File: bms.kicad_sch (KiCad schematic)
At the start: 58 parts, among them J6 TYPE-C_16PIN_2MD__073_, J7 Battery, Q2 PMOS, Q3 PMOS, U3 TPS2113ADRBR, U6 MP2639A, U8 LMV331M5, U9 LMV331M5

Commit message: changed most of the components to 0805
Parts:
- C20, C50, C51, C53: footprint Capacitor_SMD:C_0603_1608Metric_Pad1.08x0.95mm_HandSolder -> Capacitor_SMD:C_0805_2012Metric_Pad1.18x1.45mm_HandSolder
- C35, C38, C42, C43: footprint Capacitor_SMD:C_0402_1005Metric_Pad0.74x0.62mm_HandSolder -> Capacitor_SMD:C_0805_2012Metric_Pad1.18x1.45mm_HandSolder
- D3, D4, D5, D6, D7, D8: footprint LED_SMD:LED_0402_1005Metric_Pad0.77x0.64mm_HandSolder -> LED_SMD:LED_0805_2012Metric_Pad1.15x1.40mm_HandSolder
- R17, R18, R19, R20, R21, R22, R23, R24, R25, R31, R32, R33, R34, R39, R40, R41, R42, R43, R44, R45, R46, R47, R48, R49, R50, R51: footprint Resistor_SMD:R_0402_1005Metric_Pad0.72x0.64mm_HandSolder -> Resistor_SMD:R_0805_2012Metric_Pad1.20x1.40mm_HandSolder
- R26: footprint Resistor_SMD:R_0603_1608Metric_Pad0.98x0.95mm_HandSolder -> Resistor_SMD:R_0805_2012Metric_Pad1.20x1.40mm_HandSolder
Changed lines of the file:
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@@
 	)
 	(junction
+		(at 236.22 101.6)
+		(diameter 0)
+		(color 0 0 0 0)
+	)
+	(junction
 		(at 88.9 24.13)
 		(diameter 0)
@@
 	(wire
 		(pts
+			(xy 236.22 101.6) (xy 238.76 101.6)
+		)
+		(stroke
+			(width 0)
+			(type default)
+		)
+	)
+	(wire
+		(pts
 			(xy 20.32 44.45) (xy 20.32 40.64)
 		)
@@
 			)
 		)
-		(property "Footprint" "Capacitor_SMD:C_0603_1608Metric_Pad1.08x0.95mm_HandSolder"
+		(property "Footprint" "Capacitor_SMD:C_0805_2012Metric_Pad1.18x1.45mm_HandSolder"
 			(at 121.92 132.08 0)
 			(hide yes)
@@
 			)
 		)
-		(property "Footprint" "Resistor_SMD:R_0402_1005Metric_Pad0.72x0.64mm_HandSolder"
+		(property "Footprint" "Resistor_SMD:R_0805_2012Metric_Pad1.20x1.40mm_HandSolder"
 			(at 99.06 59.69 0)
 			(hide yes)
@@
 			)
 		)
-		(property "Footprint" "Resistor_SMD:R_0402_1005Metric_Pad0.72x0.64mm_HandSolder"
+		(property "Footprint" "Resistor_SMD:R_0805_2012Metric_Pad1.20x1.40mm_HandSolder"
 			(at 99.06 66.04 0)
 			(hide yes)
@@
 			)
 		)
-		(property "Footprint" "Capacitor_SMD:C_0402_1005Metric_Pad0.74x0.62mm_HandSolder"
+		(property "Footprint" "Capacitor_SMD:C_0805_2012Metric_Pad1.18x1.45mm_HandSolder"
 			(at 265.43 88.9 0)
 			(hide yes)
@@
 			)
 		)
-		(property "Footprint" "Capacitor_SMD:C_0402_1005Metric_Pad0.74x0.62mm_HandSolder"
+		(property "Footprint" "Capacitor_SMD:C_0805_2012Metric_Pad1.18x1.45mm_HandSolder"
 			(at 154.94 49.53 0)
 			(hide yes)
@@
 			)
 		)
-		(property "Footprint" "Resistor_SMD:R_0603_1608Metric_Pad0.98x0.95mm_HandSolder"
+		(property "Footprint" "Resistor_SMD:R_0805_2012Metric_Pad1.20x1.40mm_HandSolder"
 			(at 71.12 46.99 0)
 			(hide yes)
@@
 			)
 		)
-		(property "Footprint" "Capacitor_SMD:C_0402_1005Metric_Pad0.74x0.62mm_HandSolder"
+		(property "Footprint" "Capacitor_SMD:C_0805_2012Metric_Pad1.18x1.45mm_HandSolder"
 			(at 151.13 66.04 0)
 			(hide yes)
@@
 			)
 		)
-		(property "Footprint" "Resistor_SMD:R_0402_1005Metric_Pad0.72x0.64mm_HandSolder"
+		(property "Footprint" "Resistor_SMD:R_0805_2012Metric_Pad1.20x1.40mm_HandSolder"
 			(at 101.6 74.93 0)
 			(hide yes)
@@
 			)
 		)
-		(property "Footprint" "Capacitor_SMD:C_0603_1608Metric_Pad1.08x0.95mm_HandSolder"
+		(property "Footprint" "Capacitor_SMD:C_0805_2012Metric_Pad1.18x1.45mm_HandSolder"
 			(at 134.62 85.09 0)
 			(hide yes)
@@
 			)
 		)
-		(property "Footprint" "Resistor_SMD:R_0402_1005Metric_Pad0.72x0.64mm_HandSolder"
+		(property "Footprint" "Resistor_SMD:R_0805_2012Metric_Pad1.20x1.40mm_HandSolder"
 			(at 236.22 152.4 0)
 			(hide yes)
@@
 			)
 		)
-		(property "Footprint" "Resistor_SMD:R_0402_1005Metric_Pad0.72x0.64mm_HandSolder"
+		(property "Footprint" "Resistor_SMD:R_0805_2012Metric_Pad1.20x1.40mm_HandSolder"
 			(at 187.96 31.75 0)
 			(hide yes)
@@
 			)
 		)
-		(property "Footprint" "LED_SMD:LED_0402_1005Metric_Pad0.77x0.64mm_HandSolder"
+		(property "Footprint" "LED_SMD:LED_0805_2012Metric_Pad1.15x1.40mm_HandSolder"
 			(at 81.28 85.09 0)
 			(hide yes)
@@
 			)
 		)
-		(property "Footprint" "Resistor_SMD:R_0402_1005Metric_Pad0.72x0.64mm_HandSolder"
+		(property "Footprint" "Resistor_SMD:R_0805_2012Metric_Pad1.20x1.40mm_HandSolder"
 			(at 218.44 88.9 0)
 			(hide yes)
@@
 			)
 		)
-		(property "Footprint" "Resistor_SMD:R_0402_1005Metric_Pad0.72x0.64mm_HandSolder"
+		(property "Footprint" "Resistor_SMD:R_0805_2012Metric_Pad1.20x1.40mm_HandSolder"
 			(at 256.54 138.43 0)
 			(hide yes)
@@
 			)
 		)
-		(property "Footprint" "LED_SMD:LED_0402_1005Metric_Pad0.77x0.64mm_HandSolder"
+		(property "Footprint" "LED_SMD:LED_0805_2012Metric_Pad1.15x1.40mm_HandSolder"
 			(at 83.82 55.88 0)
 			(hide yes)
@@
 			)
 		)
-		(property "Footprint" "Resistor_SMD:R_0402_1005Metric_Pad0.72x0.64mm_HandSolder"
+		(property "Footprint" "Resistor_SMD:R_0805_2012Metric_Pad1.20x1.40mm_HandSolder"
 			(at 148.59 46.99 0)
 			(hide yes)
@@
 			)
 		)
-		(property "Footprint" "Resistor_SMD:R_0402_1005Metric_Pad0.72x0.64mm_HandSolder"
+		(property "Footprint" "Resistor_SMD:R_0805_2012Metric_Pad1.20x1.40mm_HandSolder"
 			(at 99.06 55.88 0)
 			(hide yes)
@@
 			)
 		)
-		(property "Footprint" "Resistor_SMD:R_0402_1005Metric_Pad0.72x0.64mm_HandSolder"
+		(property "Footprint" "Resistor_SMD:R_0805_2012Metric_Pad1.20x1.40mm_HandSolder"
 			(at 210.82 120.65 0)
 			(hide yes)
@@
 			)
 		)
-		(property "Footprint" "Resistor_SMD:R_0402_1005Metric_Pad0.72x0.64mm_HandSolder"
+		(property "Footprint" "Resistor_SMD:R_0805_2012Metric_Pad1.20x1.40mm_HandSolder"
 			(at 187.96 36.83 0)
 			(hide yes)
@@
 			)
 		)
-		(property "Footprint" "Resistor_SMD:R_0402_1005Metric_Pad0.72x0.64mm_HandSolder"
+		(property "Footprint" "Resistor_SMD:R_0805_2012Metric_Pad1.20x1.40mm_HandSolder"
 			(at 210.82 148.59 0)
 			(hide yes)
@@
 			)
 		)
-		(property "Footprint" "Resistor_SMD:R_0402_1005Metric_Pad0.72x0.64mm_HandSolder"
+		(property "Footprint" "Resistor_SMD:R_0805_2012Metric_Pad1.20x1.40mm_HandSolder"
 			(at 62.23 50.8 0)
 			(hide yes)
@@
 		(pin "9"
 		)
+		(pin "9"
+		)
 		(instances
 			(project "STM32G491RE"
@@
 			)
 		)
-		(property "Footprint" "Resistor_SMD:R_0402_1005Metric_Pad0.72x0.64mm_HandSolder"
+		(property "Footprint" "Resistor_SMD:R_0805_2012Metric_Pad1.20x1.40mm_HandSolder"
 			(at 125.73 144.78 0)
 			(hide yes)
@@
 			)
 		)
-		(property "Footprint" "LED_SMD:LED_0402_1005Metric_Pad0.77x0.64mm_HandSolder"
+		(property "Footprint" "LED_SMD:LED_0805_2012Metric_Pad1.15x1.40mm_HandSolder"
 			(at 83.82 62.23 0)
 			(hide yes)
@@
 			)
 		)
-		(property "Footprint" "Resistor_SMD:R_0402_1005Metric_Pad0.72x0.64mm_HandSolder"
+		(property "Footprint" "Resistor_SMD:R_0805_2012Metric_Pad1.20x1.40mm_HandSolder"
 			(at 236.22 124.46 0)
 			(hide yes)
@@
 			)
 		)
-		(property "Footprint" "LED_SMD:LED_0402_1005Metric_Pad0.77x0.64mm_HandSolder"
+		(property "Footprint" "LED_SMD:LED_0805_2012Metric_Pad1.15x1.40mm_HandSolder"
 			(at 83.82 66.04 0)
 			(hide yes)
@@
 			)
 		)
-		(property "Footprint" "Resistor_SMD:R_0402_1005Metric_Pad0.72x0.64mm_HandSolder"
+		(property "Footprint" "Resistor_SMD:R_0805_2012Metric_Pad1.20x1.40mm_HandSolder"
 			(at 146.05 63.5 0)
 			(hide yes)
@@
 			)
 		)
-		(property "Footprint" "Resistor_SMD:R_0402_1005Metric_Pad0.72x0.64mm_HandSolder"
+		(property "Footprint" "Resistor_SMD:R_0805_2012Metric_Pad1.20x1.40mm_HandSolder"
 			(at 161.29 64.77 0)
 			(hide yes)
@@
 			)
 		)
-		(property "Footprint" "Resistor_SMD:R_0402_1005Metric_Pad0.72x0.64mm_HandSolder"
+		(property "Footprint" "Resistor_SMD:R_0805_2012Metric_Pad1.20x1.40mm_HandSolder"
 			(at 161.29 59.69 0)
 			(hide yes)
@@
 			)
 		)
-		(property "Footprint" "Resistor_SMD:R_0402_1005Metric_Pad0.72x0.64mm_HandSolder"
+		(property "Footprint" "Resistor_SMD:R_0805_2012Metric_Pad1.20x1.40mm_HandSolder"
 			(at 250.19 132.08 0)
 			(hide yes)
@@
 			)
 		)
-		(property "Footprint" "LED_SMD:LED_0402_1005Metric_Pad0.77x0.64mm_HandSolder"
+		(property "Footprint" "LED_SMD:LED_0805_2012Metric_Pad1.15x1.40mm_HandSolder"
 			(at 81.28 80.01 0)
 			(hide yes)
@@
 			)
 		)
-		(property "Footprint" "Resistor_SMD:R_0402_1005Metric_Pad0.72x0.64mm_HandSolder"
+		(property "Footprint" "Resistor_SMD:R_0805_2012Metric_Pad1.20x1.40mm_HandSolder"
 			(at 181.61 128.27 0)
 			(hide yes)
@@
 			)
 		)
-		(property "Footprint" "Capacitor_SMD:C_0603_1608Metric_Pad1.08x0.95mm_HandSolder"
+		(property "Footprint" "Capacitor_SMD:C_0805_2012Metric_Pad1.18x1.45mm_HandSolder"
 			(at 88.9 21.59 0)
 			(hide yes)
@@
 			)
 		)
-		(property "Footprint" "Resistor_SMD:R_0402_1005Metric_Pad0.72x0.64mm_HandSolder"
+		(property "Footprint" "Resistor_SMD:R_0805_2012Metric_Pad1.20x1.40mm_HandSolder"
 			(at 163.83 144.78 0)
 			(hide yes)
@@
 			)
 		)
-		(property "Footprint" "Resistor_SMD:R_0402_1005Metric_Pad0.72x0.64mm_HandSolder"
+		(property "Footprint" "Resistor_SMD:R_0805_2012Metric_Pad1.20x1.40mm_HandSolder"
 			(at 105.41 76.2 0)
 			(hide yes)
@@
 			)
 		)
-		(property "Footprint" "LED_SMD:LED_0402_1005Metric_Pad0.77x0.64mm_HandSolder"
+		(property "Footprint" "LED_SMD:LED_0805_2012Metric_Pad1.15x1.40mm_HandSolder"
 			(at 83.82 59.69 0)
 			(hide yes)
@@
 			)
 		)
-		(property "Footprint" "Capacitor_SMD:C_0402_1005Metric_Pad0.74x0.62mm_HandSolder"
+		(property "Footprint" "Capacitor_SMD:C_0805_2012Metric_Pad1.18x1.45mm_HandSolder"
 			(at 257.81 88.9 0)
 			(hide yes)
@@
 			)
 		)
-		(property "Footprint" "Resistor_SMD:R_0402_1005Metric_Pad0.72x0.64mm_HandSolder"
+		(property "Footprint" "Resistor_SMD:R_0805_2012Metric_Pad1.20x1.40mm_HandSolder"
 			(at 146.05 66.04 0)
 			(hide yes)
@@
 			)
 		)
-		(property "Footprint" "Resistor_SMD:R_0402_1005Metric_Pad0.72x0.64mm_HandSolder"
+		(property "Footprint" "Resistor_SMD:R_0805_2012Metric_Pad1.20x1.40mm_HandSolder"
 			(at 181.61 133.35 0)
 			(hide yes)
@@
 			)
 		)
-		(property "Footprint" "Resistor_SMD:R_0402_1005Metric_Pad0.72x0.64mm_HandSolder"
+		(property "Footprint" "Resistor_SMD:R_0805_2012Metric_Pad1.20x1.40mm_HandSolder"
 			(at 99.06 62.23 0)
 			(hide yes)
@@
 			)
 		)
-		(property "Footprint" "Resistor_SMD:R_0402_1005Metric_Pad0.72x0.64mm_HandSolder"
+		(property "Footprint" "Resistor_SMD:R_0805_2012Metric_Pad1.20x1.40mm_HandSolder"
 			(at 148.59 44.45 0)
 			(hide yes)
@@
 			)
 		)
-		(property "Footprint" "Capacitor_SMD:C_0603_1608Metric_Pad1.08x0.95mm_HandSolder"
+		(property "Footprint" "Capacitor_SMD:C_0805_2012Metric_Pad1.18x1.45mm_HandSolder"
 			(at 36.83 46.99 0)
 			(hide yes)

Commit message: finalized parts before sensors
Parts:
- removed C59: 22uF, Capacitor_SMD:C_1206_3216Metric_Pad1.33x1.80mm_HandSolder, symbol Device:C_Small
- C51: footprint Capacitor_SMD:C_0805_2012Metric_Pad1.18x1.45mm_HandSolder -> Capacitor_SMD:C_0603_1608Metric_Pad1.08x0.95mm_HandSolder
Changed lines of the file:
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@@
 	)
 	(junction
-		(at 29.21 40.64)
-		(diameter 0)
-		(color 0 0 0 0)
-	)
-	(junction
 		(at 121.92 129.54)
 		(diameter 0)
@@
 	(wire
 		(pts
-			(xy 20.32 49.53) (xy 20.32 54.61)
-		)
-		(stroke
-			(width 0)
-			(type default)
-		)
-	)
-	(wire
-		(pts
 			(xy 57.15 54.61) (xy 62.23 54.61)
 		)
@@
 	(wire
 		(pts
-			(xy 20.32 40.64) (xy 29.21 40.64)
-		)
-		(stroke
-			(width 0)
-			(type default)
-		)
-	)
-	(wire
-		(pts
 			(xy 143.51 22.86) (xy 148.59 22.86)
 		)
@@
 	(wire
 		(pts
-			(xy 20.32 44.45) (xy 20.32 40.64)
-		)
-		(stroke
-			(width 0)
-			(type default)
-		)
-	)
-	(wire
-		(pts
 			(xy 76.2 85.09) (xy 77.47 85.09)
 		)
@@
 	)
 	(symbol
-		(lib_id "Device:C_Small")
-		(at 20.32 46.99 0)
-		(mirror y)
-		(unit 1)
-		(body_style 1)
-		(exclude_from_sim no)
-		(in_bom yes)
-		(on_board yes)
-		(in_pos_files yes)
-		(dnp no)
-		(property "Reference" "C59"
-			(at 18.034 47.752 0)
-			(show_name no)
-			(do_not_autoplace no)
-			(effects
-				(font
-					(size 1.27 1.27)
-				)
-				(justify left)
-			)
-		)
-		(property "Value" "22uF"
-			(at 18.542 45.974 0)
-			(show_name no)
-			(do_not_autoplace no)
-			(effects
-				(font
-					(size 1.27 1.27)
-				)
-				(justify left)
-			)
-		)
-		(property "Footprint" "Capacitor_SMD:C_1206_3216Metric_Pad1.33x1.80mm_HandSolder"
-			(at 20.32 46.99 0)
-			(hide yes)
-			(show_name no)
-			(do_not_autoplace no)
-			(effects
-				(font
-					(size 1.27 1.27)
-				)
-			)
-		)
-		(property "Datasheet" ""
-			(at 20.32 46.99 0)
-			(hide yes)
-			(show_name no)
-			(do_not_autoplace no)
-			(effects
-				(font
-					(size 1.27 1.27)
-				)
-			)
-		)
-		(property "Description" "Unpolarized capacitor, small symbol"
-			(at 20.32 46.99 0)
-			(hide yes)
-			(show_name no)
-			(do_not_autoplace no)
-			(effects
-				(font
-					(size 1.27 1.27)
-				)
-			)
-		)
-		(pin "1"
-		)
-		(pin "2"
-		)
-		(instances
-			(project "STM32G491RE"
-				(path "/213f8898-394f-49c4-9e4a-d0dfd12ebcad/e9a9bd6d-d0b2-41a1-a6d5-2085ebfa0e2e"
-					(reference "C59")
-					(unit 1)
-				)
-			)
-		)
-	)
-	(symbol
 		(lib_id "power:GND")
 		(at 218.44 91.44 0)
@@
 	)
 	(symbol
-		(lib_id "power:GND")
-		(at 20.32 54.61 0)
-		(unit 1)
-		(body_style 1)
-		(exclude_from_sim no)
-		(in_bom yes)
-		(on_board yes)
-		(in_pos_files yes)
-		(dnp no)
-		(property "Reference" "#PWR0118"
-			(at 20.32 60.96 0)
-			(hide yes)
-			(show_name no)
-			(do_not_autoplace no)
-			(effects
-				(font
-					(size 1.27 1.27)
-				)
-			)
-		)
-		(property "Value" "GND"
-			(at 20.32 58.166 0)
-			(show_name no)
-			(do_not_autoplace no)
-			(effects
-				(font
-					(size 1.27 1.27)
-				)
-			)
-		)
-		(property "Footprint" ""
-			(at 20.32 54.61 0)
-			(hide yes)
-			(show_name no)
-			(do_not_autoplace no)
-			(effects
-				(font
-					(size 1.27 1.27)
-				)
-			)
-		)
-		(property "Datasheet" ""
-			(at 20.32 54.61 0)
-			(hide yes)
-			(show_name no)
-			(do_not_autoplace no)
-			(effects
-				(font
-					(size 1.27 1.27)
-				)
-			)
-		)
-		(property "Description" "Power symbol creates a global label with name \"GND\" , ground"
-			(at 20.32 54.61 0)
-			(hide yes)
-			(show_name no)
-			(do_not_autoplace no)
-			(effects
-				(font
-					(size 1.27 1.27)
-				)
-			)
-		)
-		(pin "1"
-		)
-		(instances
-			(project "STM32G491RE"
-				(path "/213f8898-394f-49c4-9e4a-d0dfd12ebcad/e9a9bd6d-d0b2-41a1-a6d5-2085ebfa0e2e"
-					(reference "#PWR0118")
-					(unit 1)
-				)
-			)
-		)
-	)
-	(symbol
 		(lib_id "Device:R_Small")
 		(at 105.41 76.2 0)
@@
 			)
 		)
-		(property "Footprint" "Capacitor_SMD:C_0805_2012Metric_Pad1.18x1.45mm_HandSolder"
+		(property "Footprint" "Capacitor_SMD:C_0603_1608Metric_Pad1.08x0.95mm_HandSolder"
 			(at 36.83 46.99 0)
 			(hide yes)

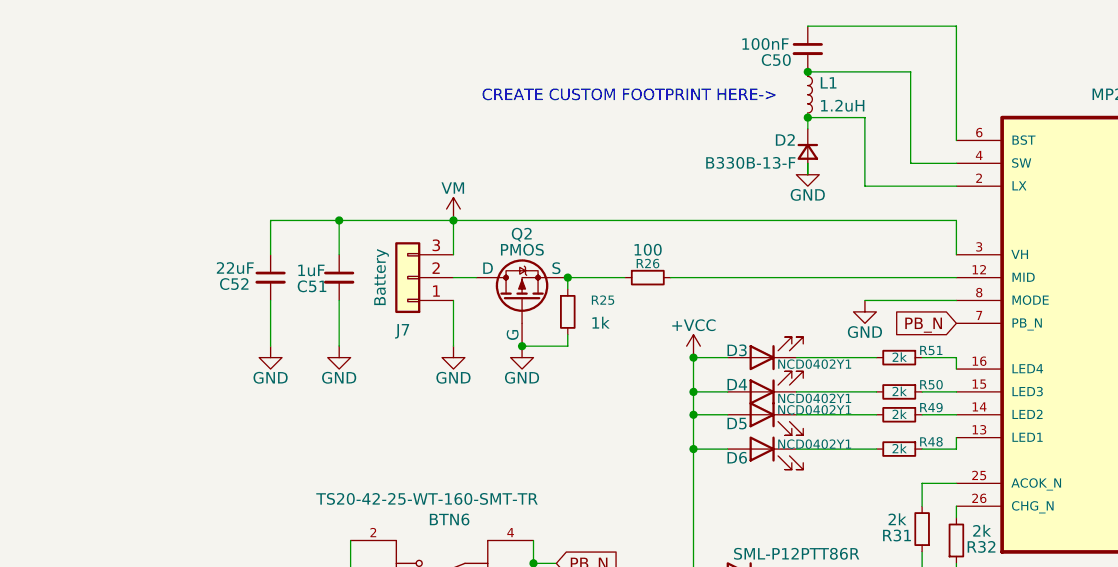
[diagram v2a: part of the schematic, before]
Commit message: fixed sensor schematic and begun pcb layout
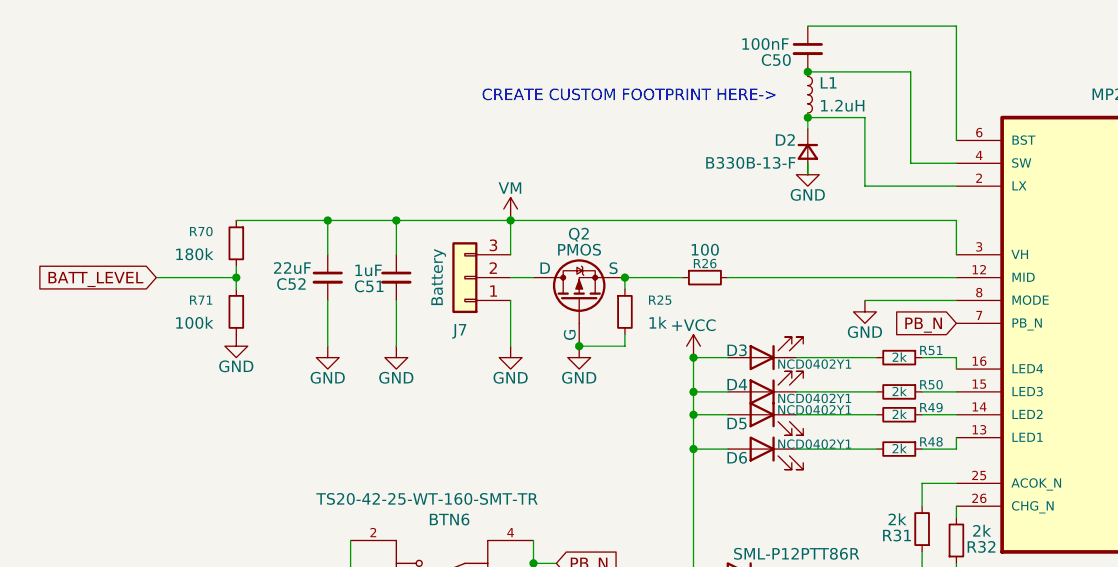
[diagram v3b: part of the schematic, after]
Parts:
- added R70: 180k, Resistor_SMD:R_0805_2012Metric_Pad1.20x1.40mm_HandSolder, symbol Device:R_Small
- added R71: 100k, Resistor_SMD:R_0805_2012Metric_Pad1.20x1.40mm_HandSolder, symbol Device:R_Small
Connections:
- net GND: now also R71.2
- net VM: now also R70.1
- new net BATT_LEVEL: R70.2, R71.1
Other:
- moved on the sheet: C51, C52, J7, Q2, R25, R26

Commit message: slightly change schematic, making sure everything is ok, preparing for finalization
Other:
- note removed: "CREATE CUSTOM FOOTPRINT HERE->"
- note removed: "divider 180k / 100k gives us 3V at 8.4V input"
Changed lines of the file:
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@@
-		)
-	)
-	(text "divider 180k / 100k gives us 3V at 8.4V input\n"
-		(exclude_from_sim no)
-		(at 90.678 102.108 0)
-		(effects
-			(font
-				(size 1.27 1.27)
-			)
 		)
 	)
@@
 		(effects
 			(font
-				(size 1.27 1.27)
-			)
-		)
-	)
-	(text "CREATE CUSTOM FOOTPRINT HERE->"
-		(exclude_from_sim no)
-		(at 69.088 26.924 0)
-		(effects
-			(font
